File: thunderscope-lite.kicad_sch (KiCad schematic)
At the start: 1 part, among them U2 AD9288BSTZ-40

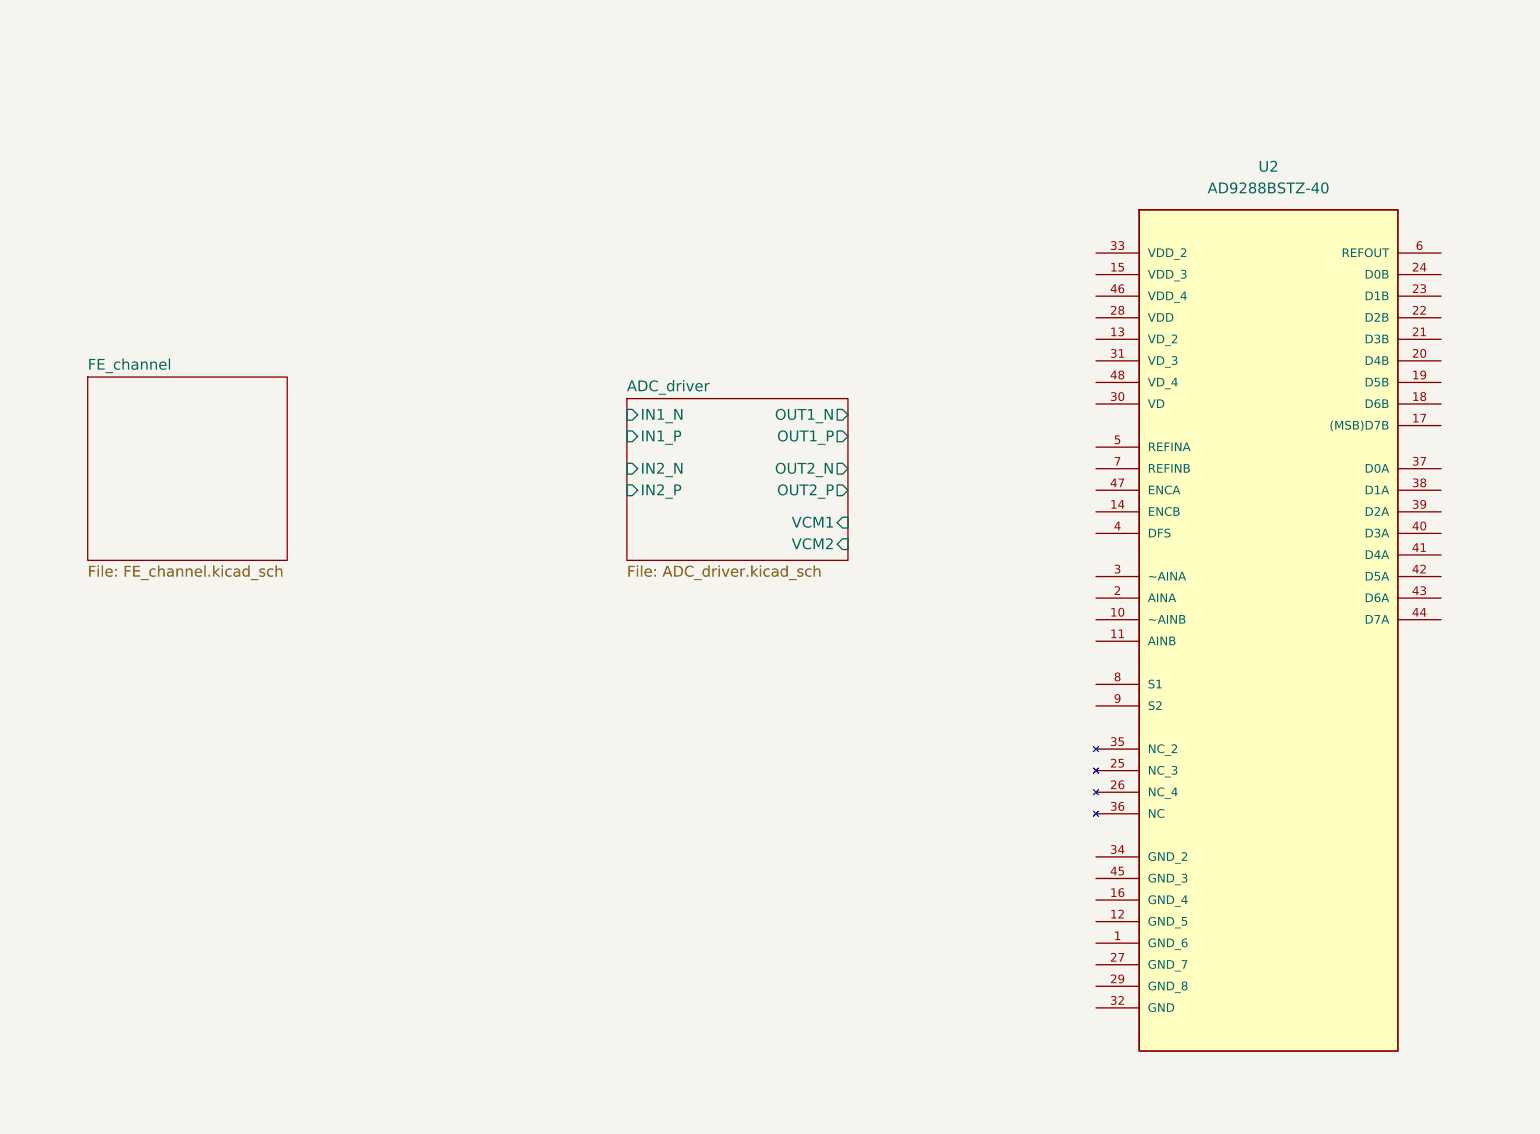
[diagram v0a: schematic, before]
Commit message: finished the FE channel and voltage generation
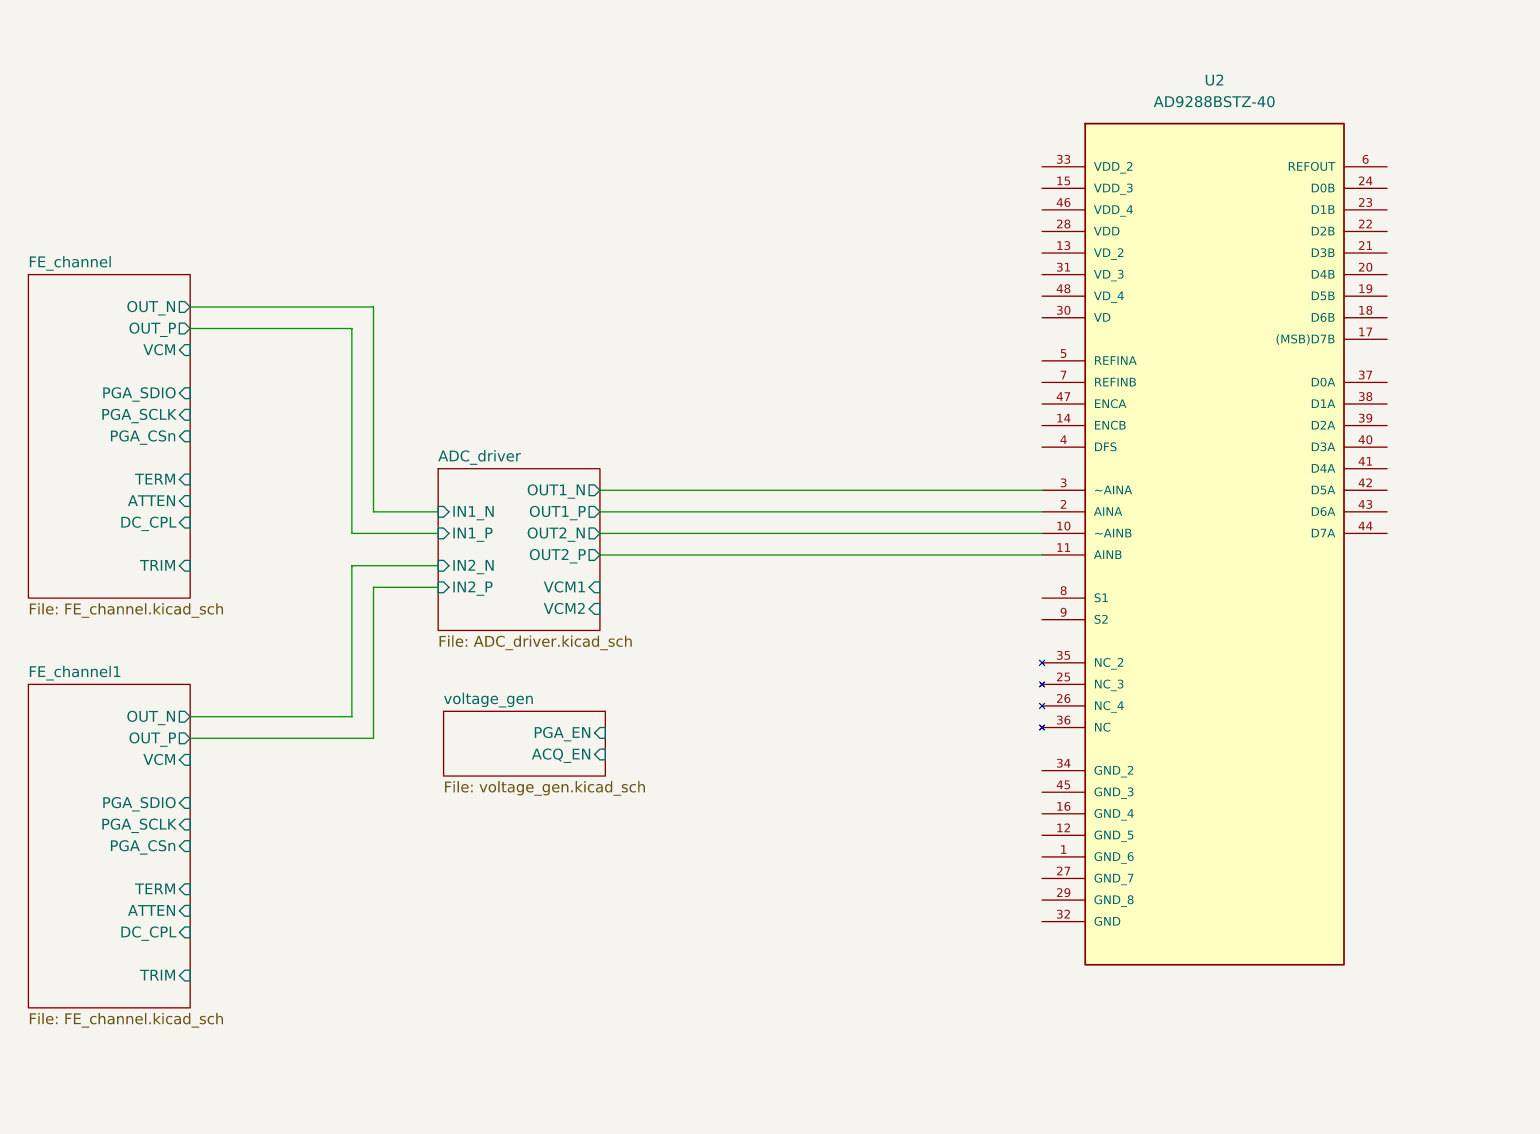
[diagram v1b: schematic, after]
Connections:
- net ADC_driver/OUT1_N: now also U2.3 (~AINA)
- net ADC_driver/OUT1_P: now also U2.2 (AINA)
- net ADC_driver/OUT2_N: now also U2.10 (~AINB)
- net ADC_driver/OUT2_P: now also U2.11 (AINB)
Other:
- added sheet FE_channel1 (FE_channel.kicad_sch)
- added sheet voltage_gen (voltage_gen.kicad_sch)
- sheet FE_channel ports: added ATTEN, DC_CPL, OUT_N, OUT_P, PGA_CSn, PGA_SCLK, PGA_SDIO, TERM, TRIM, VCM; removed none
- moved on the sheet: U2

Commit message: added ADC, added FE trim. now all that's left is the micromicrocontroller
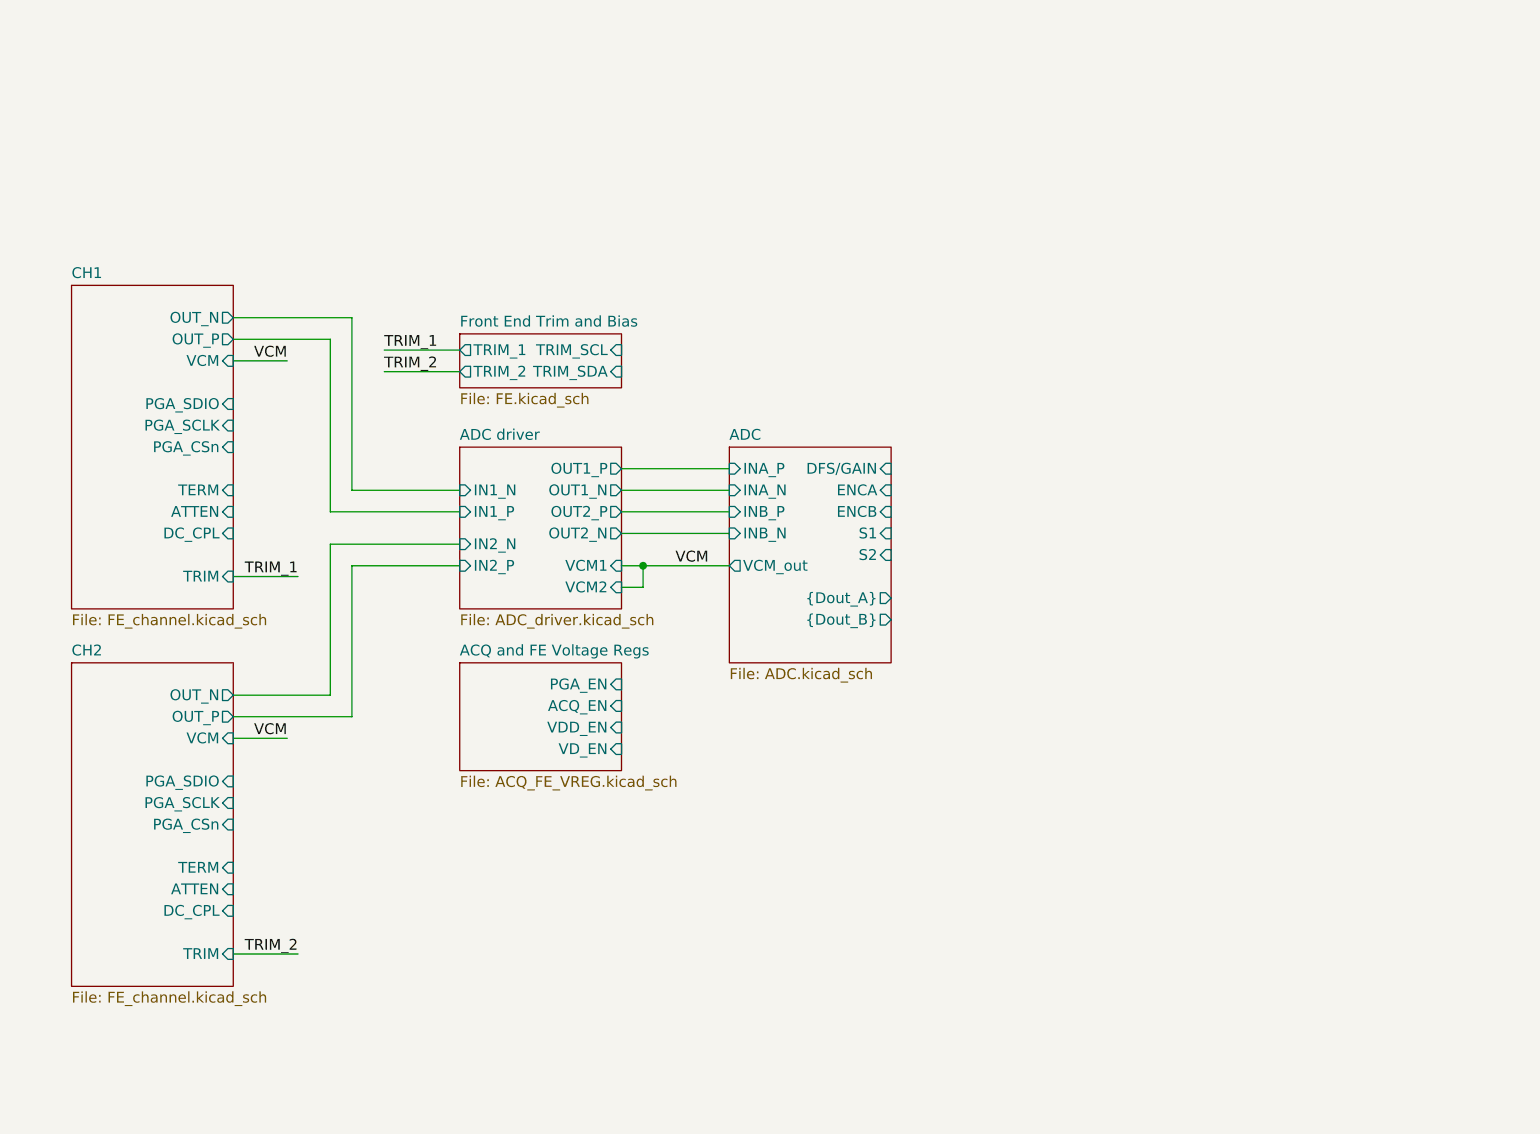
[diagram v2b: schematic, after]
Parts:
- removed U2: AD9288BSTZ-40, AD9288BSTZ-40:QFP50P900X900X160-48N, symbol AD9288BSTZ-40:AD9288BSTZ-40
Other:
- sheet ADC_driver renamed ADC driver
- sheet FE_channel renamed CH1
- sheet FE_channel1 renamed CH2
- sheet voltage_gen renamed ACQ and FE Voltage Regs
- added sheet ADC (ADC.kicad_sch)
- added sheet Front End Trim and Bias (FE.kicad_sch)
- sheet ACQ and FE Voltage Regs: file voltage_gen.kicad_sch -> ACQ_FE_VREG.kicad_sch
- sheet ACQ and FE Voltage Regs ports: added VDD_EN, VD_EN; removed none

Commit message: decided on clk source and MCU
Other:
- added sheet CLK Source (CLK.kicad_sch)
- added sheet MCU (MCU.kicad_sch)
- sheet ADC ports: added ENC; removed ENCA, ENCB
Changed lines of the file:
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@@
+	(wire
+		(pts
+			(xy 158.75 74.93) (xy 171.45 74.93)
+		)
+		(stroke
+			(width 0)
+			(type default)
+		)
+	)
 	(wire
 		(pts
@@
 	)
 	(sheet
+		(at 171.45 72.39)
+		(size 12.7 5.08)
+		(exclude_from_sim no)
+		(in_bom yes)
+		(on_board yes)
+		(dnp no)
+		(fields_autoplaced yes)
+		(stroke
+			(width 0.1524)
+			(type solid)
+		)
+		(fill
+			(color 0 0 0 0.0000)
+		)
+		(property "Sheetname" "CLK Source"
+			(at 171.45 71.6784 0)
+			(effects
+				(font
+					(size 1.27 1.27)
+				)
+				(justify left bottom)
+			)
+		)
+		(property "Sheetfile" "CLK.kicad_sch"
+			(at 171.45 78.0546 0)
+			(effects
+				(font
+					(size 1.27 1.27)
+				)
+				(justify left top)
+			)
+		)
+		(pin "XO_CLK" output
+			(at 171.45 74.93 180)
+			(effects
+				(font
+					(size 1.27 1.27)
+				)
+				(justify left)
+			)
+		)
+		(instances
+			(project "thunderscope-lite"
+				(path "/920a8b65-6ec2-414c-bfee-6322de42233d"
+					(page "9")
+				)
+			)
+		)
+	)
+	(sheet
+		(at 196.85 69.85)
+		(size 12.7 12.7)
+		(exclude_from_sim no)
+		(in_bom yes)
+		(on_board yes)
+		(dnp no)
+		(fields_autoplaced yes)
+		(stroke
+			(width 0.1524)
+			(type solid)
+		)
+		(fill
+			(color 0 0 0 0.0000)
+		)
+		(property "Sheetname" "MCU"
+			(at 196.85 69.1384 0)
+			(effects
+				(font
+					(size 1.27 1.27)
+				)
+				(justify left bottom)
+			)
+		)
+		(property "Sheetfile" "MCU.kicad_sch"
+			(at 196.85 83.1346 0)
+			(effects
+				(font
+					(size 1.27 1.27)
+				)
+				(justify left top)
+			)
+		)
+		(instances
+			(project "thunderscope-lite"
+				(path "/920a8b65-6ec2-414c-bfee-6322de42233d"
+					(page "8")
+				)
+			)
+		)
+	)
+	(sheet
 		(at 62.23 50.8)
 		(size 19.05 38.1)
@@
 	(sheet
 		(at 139.7 69.85)
-		(size 19.05 25.4)
+		(size 19.05 19.05)
 		(exclude_from_sim no)
 		(in_bom yes)
@@
 		)
 		(property "Sheetfile" "ADC.kicad_sch"
-			(at 139.7 95.8346 0)
+			(at 139.7 89.4846 0)
 			(effects
 				(font
@@
 			)
 		)
-		(pin "ENCA" input
-			(at 158.75 74.93 0)
-			(effects
-				(font
-					(size 1.27 1.27)
-				)
-				(justify right)
-			)
-		)
-		(pin "ENCB" input
-			(at 158.75 77.47 0)
-			(effects
-				(font
-					(size 1.27 1.27)
-				)
-				(justify right)
-			)
-		)
 		(pin "INA_N" input
 			(at 139.7 74.93 180)
@@
 		)
 		(pin "S1" input
+			(at 158.75 77.47 0)
+			(effects
+				(font
+					(size 1.27 1.27)
+				)
+				(justify right)
+			)
+		)
+		(pin "S2" input
 			(at 158.75 80.01 0)
-			(effects
-				(font
-					(size 1.27 1.27)
-				)
-				(justify right)
-			)
-		)
-		(pin "S2" input
-			(at 158.75 82.55 0)
 			(effects
 				(font
@@
 		)
 		(pin "{Dout_A}" output
-			(at 158.75 87.63 0)
+			(at 158.75 82.55 0)
 			(effects
 				(font
@@
 		)
 		(pin "{Dout_B}" output
-			(at 158.75 90.17 0)
-			(effects
-				(font
+			(at 158.75 85.09 0)
+			(effects
+				(font
+					(size 1.27 1.27)
+				)
+				(justify right)
+			)
+		)
+		(pin "ENC" input
+			(at 158.75 74.93 0)
+			(effects
+				(font

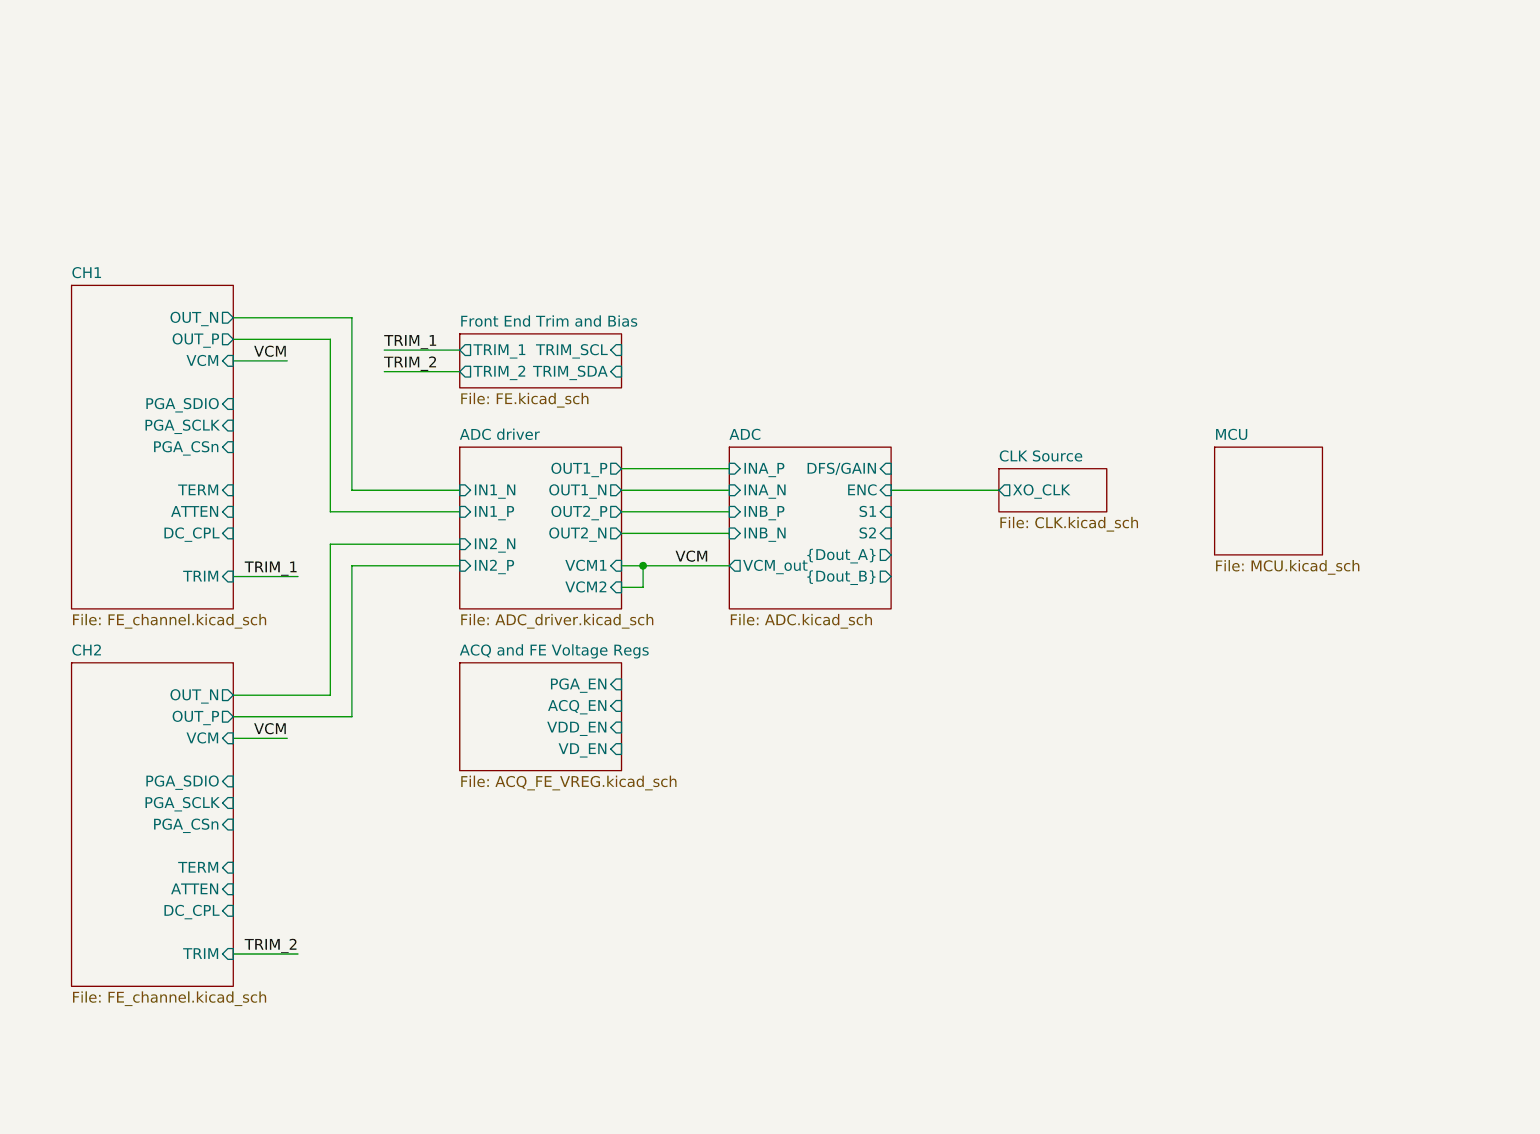
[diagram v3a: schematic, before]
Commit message: almost done with the microcontroller, just need to connect t the AFE and ADC pins
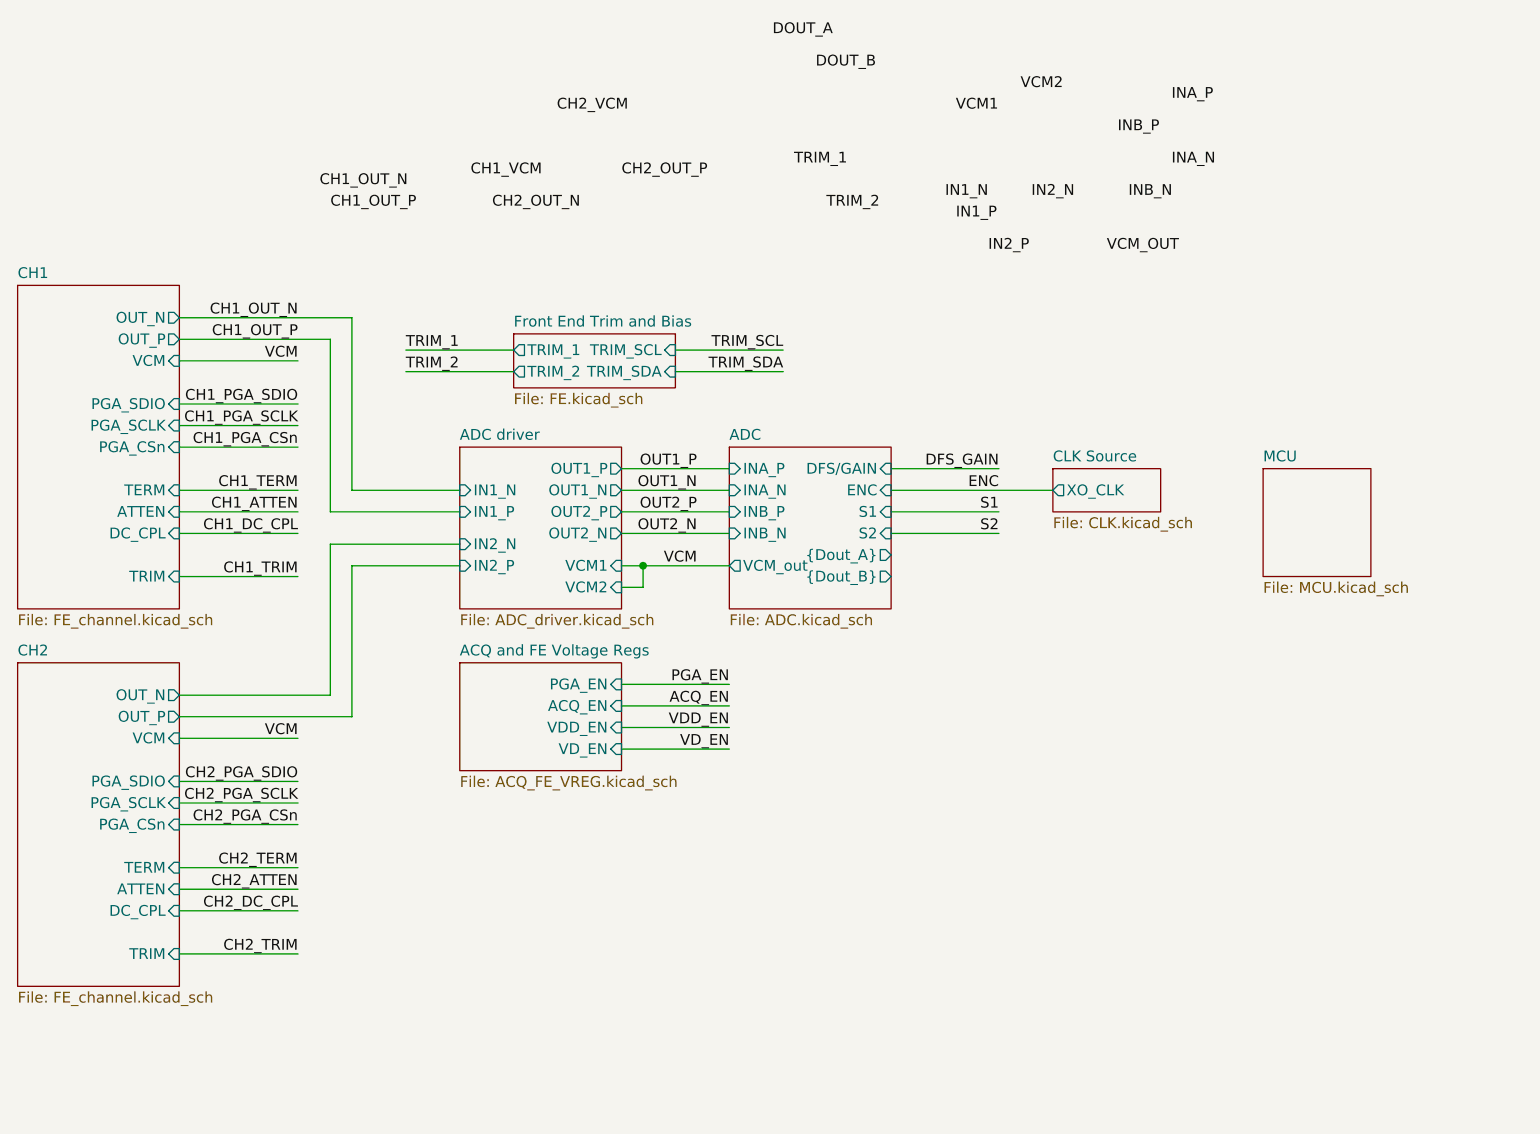
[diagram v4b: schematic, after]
